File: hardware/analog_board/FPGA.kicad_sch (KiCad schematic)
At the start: 12 parts, among them U1 GW2A-LV18EQ144

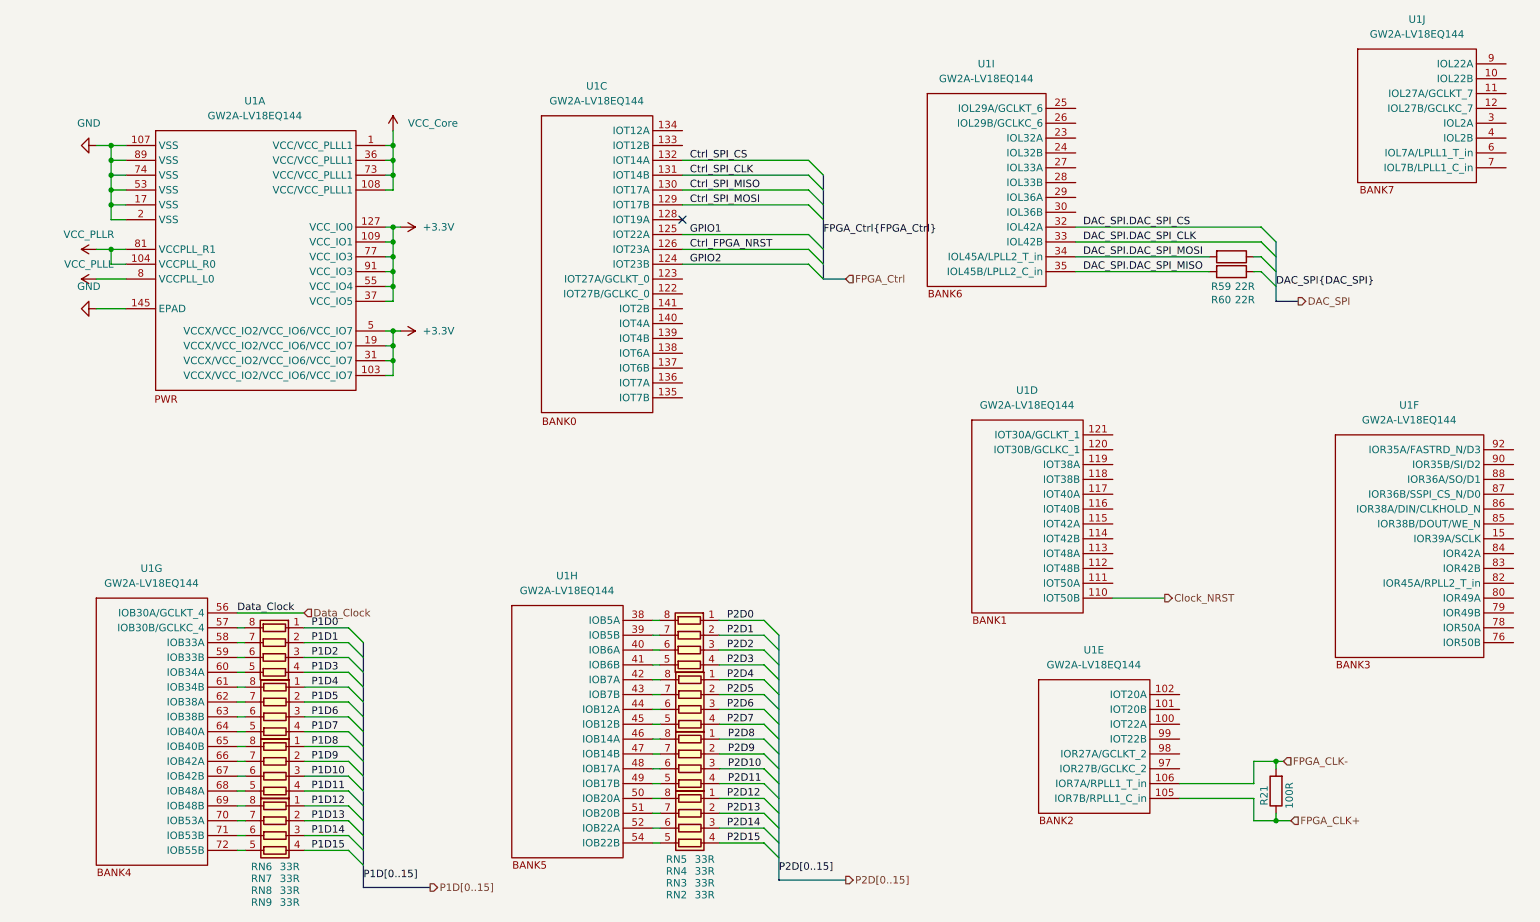
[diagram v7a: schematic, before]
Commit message: feat：根据PCB微调原理图
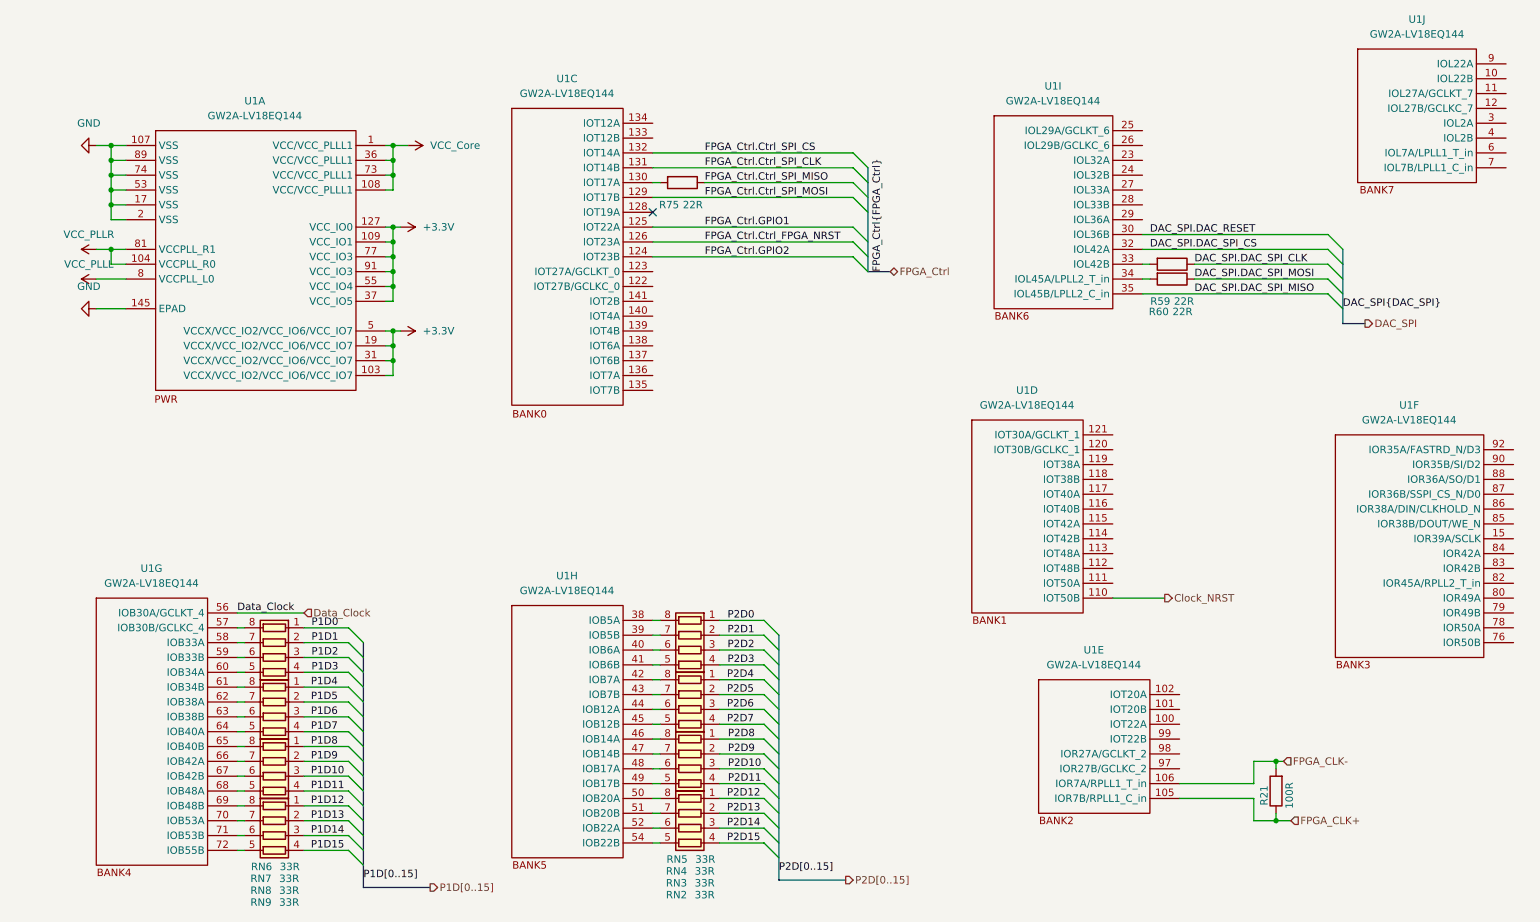
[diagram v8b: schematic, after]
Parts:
- added R75: 22R, Resistor_SMD:R_0402_1005Metric, symbol Device:R
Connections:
- net DAC_SPI.DAC_SPI_CLK: now also R59.1; no longer U1.33 (IOL42B)
- net DAC_SPI.DAC_SPI_MISO: no longer R60.2
- net DAC_SPI.DAC_SPI_MOSI: now also R60.1; no longer R59.2, U1.34 (IOL45A/LPLL2_T_in)
- net DAC_SPI.DAC_RESET: now reaches U1.30 (IOL36B)
- net Ctrl_FPGA_NRST renamed FPGA_Ctrl.Ctrl_FPGA_NRST
- net Ctrl_SPI_CLK renamed FPGA_Ctrl.Ctrl_SPI_CLK
- net Ctrl_SPI_CS renamed FPGA_Ctrl.Ctrl_SPI_CS
- net Ctrl_SPI_MISO: no longer names the net of U1.130 (IOT17A)
- net Ctrl_SPI_MISO: now also R75.2
- net Ctrl_SPI_MOSI renamed FPGA_Ctrl.Ctrl_SPI_MOSI
- net GPIO1 renamed FPGA_Ctrl.GPIO1
- net GPIO2 renamed FPGA_Ctrl.GPIO2
- new net: R59.2, U1.33 (IOL42B)
- new net: R60.2, U1.34 (IOL45A/LPLL2_T_in)
- new net FPGA_Ctrl.Ctrl_SPI_MISO: R75.1
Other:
- moved on the sheet: U1C, U1I
